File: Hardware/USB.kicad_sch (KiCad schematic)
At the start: 14 parts, among them J5 USB4120-03-C, U8 CP2102N-A02-GQFN24

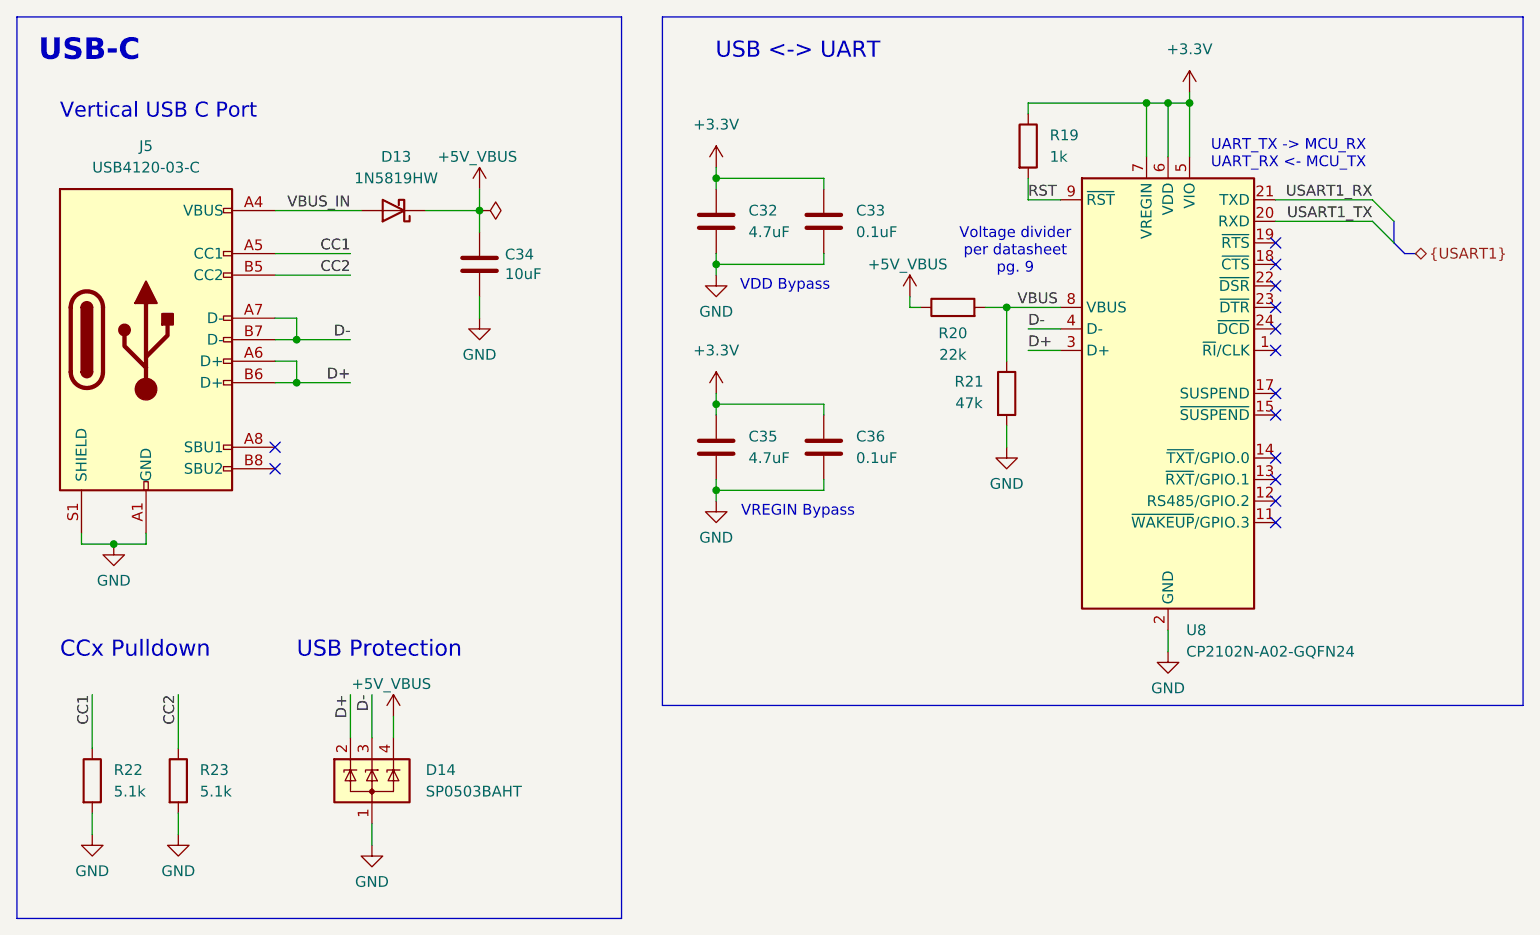
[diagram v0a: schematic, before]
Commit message: RevB Changes (#4)
* added documentation for current range; added VBUS led

* INA common-mode fixed (i think)

* differential amp for LPF

* diff amp / LPF

* some comments so I don't forget what I'm doing

* new TLV symbol, SPDT switch for scrut

* fixed LPF cutoff

* refactored and added LPF docs; added fuse, boot_gpio from USB-UART chip

* i lowk haven't started layout

* slightly cooked

* started layout not really but kind of

* layout stuff

* post review council sch changes: shielded connectors, removed SHDN resistor, diode OR for boot, standardized resistors

* starting routing i think

* almost done with routing

* wow

* drc is happy

* ye

* again

* addressed some comments

* added lcsc part numbers

* generated production files and docs

* updated STEP file

* symbol library

* addressed comments; generated production files, docs

* added Mouser BOM, deleted embedded step files
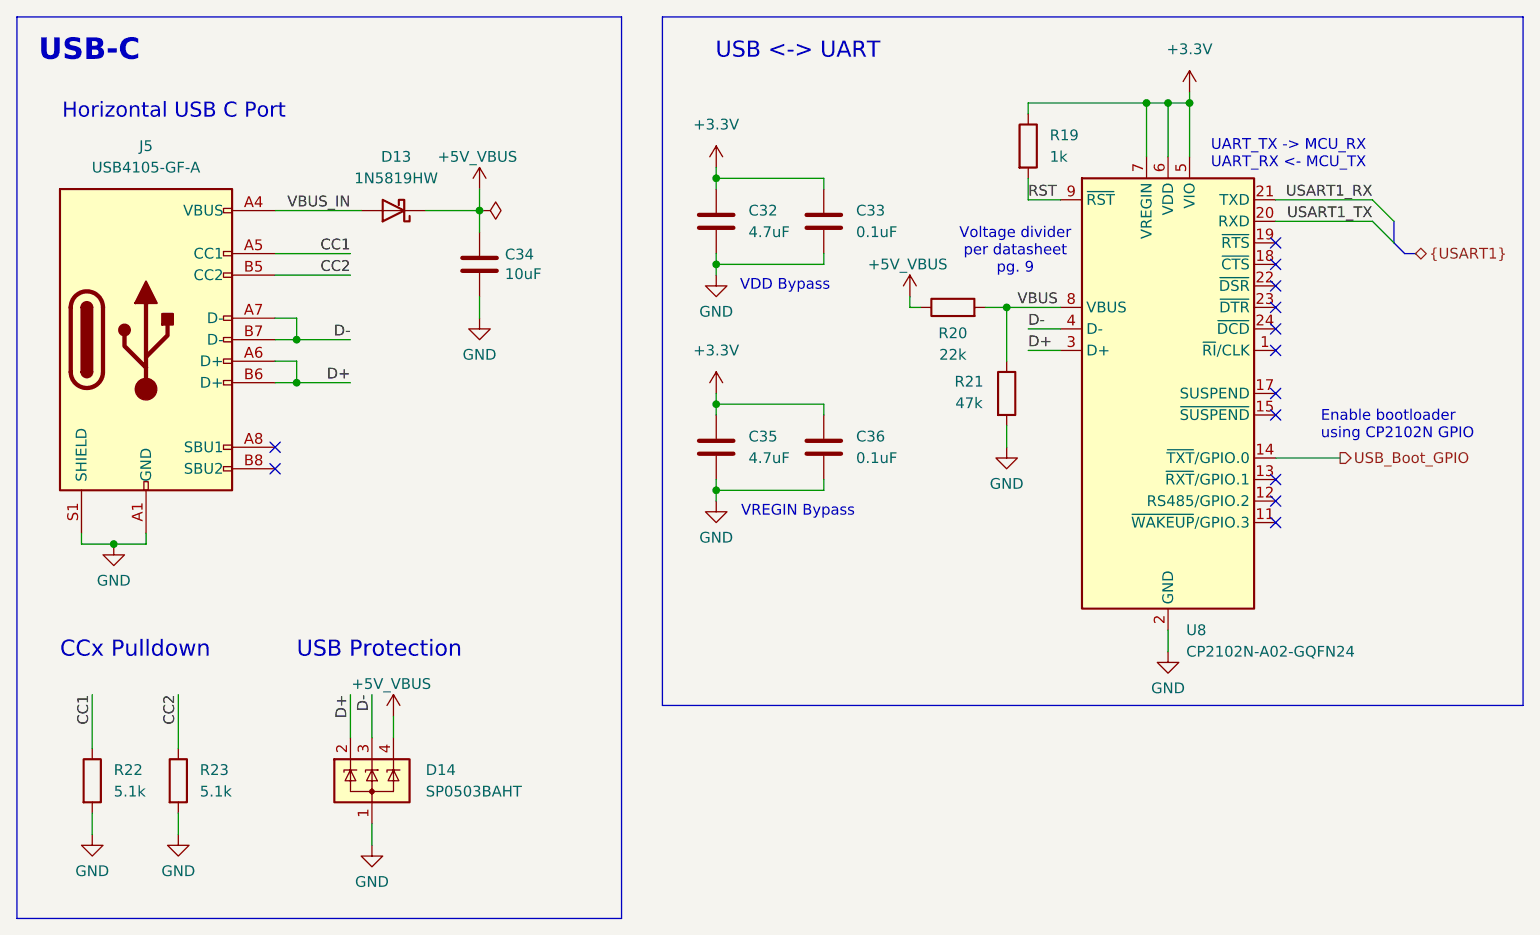
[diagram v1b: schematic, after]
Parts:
- J5: value USB4120-03-C -> USB4105-GF-A; footprint Parts:USB412003C -> UTSVT_Connectors:USB_C_Receptacle_GCT_USB4105-xx-A_16P_TopMnt_Horizontal; P/N USB4120-03-C -> USB4105-GF-A
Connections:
- net USB_Boot_GPIO: now reaches U8.14 (~{TXT}/GPIO.0)
- no-connect marks 14 -> 13
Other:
- note added: "Enable bootloader using CP2102N GPIO"
- note added: "Horizontal USB C Port"
- note removed: "Vertical USB C Port"
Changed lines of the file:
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@@
 		)
 	)
-	(text "Vertical USB C Port"
-		(exclude_from_sim no)
-		(at 20.32 25.4 0)
+	(text "Horizontal USB C Port"
+		(exclude_from_sim no)
+		(at 20.574 25.4 0)
 		(effects
 			(font
 				(size 1.778 1.778)
+			)
+			(justify left top)
+		)
+	)
+	(text "Enable bootloader \nusing CP2102N GPIO"
+		(exclude_from_sim no)
+		(at 169.164 61.722 0)
+		(effects
+			(font
+				(size 1.27 1.27)
 			)
 			(justify left top)
@@
 	)
 	(no_connect
-		(at 163.83 67.31)
-	)
-	(no_connect
 		(at 163.83 49.53)
 	)
@@
 		(pts
 			(xy 134.62 25.4) (xy 148.59 25.4)
+		)
+		(stroke
+			(width 0)
+			(type default)
+		)
+	)
+	(wire
+		(pts
+			(xy 163.83 67.31) (xy 171.45 67.31)
 		)
 		(stroke
@@
 		)
 	)
+	(hierarchical_label "USB_Boot_GPIO"
+		(shape output)
+		(at 171.45 67.31 0)
+		(effects
+			(font
+				(size 1.27 1.27)
+			)
+			(justify left)
+		)
+	)
 	(symbol
 		(lib_id "Device:R")
@@
 			)
 		)
-		(property "Value" "USB4120-03-C"
+		(property "Value" "USB4105-GF-A"
 			(at 30.48 33.02 0)
 			(effects
@@
 			)
 		)
-		(property "Footprint" "Parts:USB412003C"
+		(property "Footprint" "UTSVT_Connectors:USB_C_Receptacle_GCT_USB4105-xx-A_16P_TopMnt_Horizontal"
 			(at 34.29 53.34 0)
 			(effects
@@
 			)
 		)
-		(property "Datasheet" "https://www.mouser.com/catalog/specsheets/GCT_USB4120.pdf"
+		(property "Datasheet" "https://www.mouser.com/ProductDetail/GCT/USB4105-GF-A?qs=KUoIvG%2F9IlY%2FMLlBMpStpA%3D%3D"
 			(at 34.29 53.34 0)
 			(effects
@@
 			)
 		)
-		(property "P/N" "USB4120-03-C"
+		(property "P/N" "USB4105-GF-A"
 			(at 30.48 53.34 0)
 			(effects
